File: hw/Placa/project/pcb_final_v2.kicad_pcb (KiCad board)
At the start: 2 copper layers, 22 parts, among them J1 pin_socket-bluepill, J10 tcrt5000_conector_2, J11 tcrt5000_conector_3, J12 tcrt5000_conector_1, J2 pin_socket-bluepill, J9 tof-connector_3, SW2 key, U2 Receptor IR, U4 AMS1117-3.3

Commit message: atualização pcb
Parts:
- removed power_drive1: KRE borne, TerminalBlock_Phoenix:TerminalBlock_Phoenix_MKDS-1,5-2-5.08_1x02_P5.08mm_Horizontal
- moved C2 22.2 mm to (128.0, 68.5), turned to -90 degrees
- moved U4 20.9 mm to (118.0, 72.3)
- moved C_polarized1 17.7 mm to (132.5, 69.5), turned to 90 degrees
- moved D1 14.3 mm to (128.9, 64.0), turned to 90 degrees
- moved L1 9.82 mm to (139.5, 69.5)
- moved D3 9.49 mm to (143.4, 69.5)
- moved C3 9.39 mm to (126.5, 78.5)
- moved SW2 7.29 mm to (134.5, 64.0), turned to 90 degrees
- moved J2 6.86 mm to (147.3, 79.9)
- moved OUT_buck-6V1 2.61 mm to (159.5, 58.5)
- moved IN_buck-7.4V1 2.25 mm to (147.0, 58.5)
- moved J9 1.52 mm to (161.5, 75.8)
- moved tof-connector_2 1.52 mm to (161.5, 95.2)
- moved signal_motors1 1.36 mm to (127.0, 126.5)
- moved J1 1.32 mm to (132.1, 79.9)
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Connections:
- OUT_buck-6V1 pad 1: GNDPWR -> GNDS
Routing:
- net (no net): track 0.00 -> 197.9 mm
- net GNDPWR: track 112.0 -> 38.6 mm
- net I2C1_SCL: track 69.4 -> 0.00 mm, vias 4 -> 0
- net I2C1_SDA: track 68.5 -> 0.00 mm, vias 5 -> 0
- net GNDS: track 138.8 -> 92.3 mm, vias 3 -> 0
- net +3V3: track 142.7 -> 97.2 mm, vias 11 -> 1
- net XSHUT1: track 31.6 -> 0.00 mm
- net XSHUT3: track 27.2 -> 0.00 mm
- net XSHUT2: track 24.8 -> 0.00 mm
- net D4: track 24.6 -> 0.00 mm
- net MB-: track 22.7 -> 0.00 mm
- net IN-BUCK: track 28.4 -> 8.30 mm
- net MB+: track 19.1 -> 0.00 mm
- net D1: track 17.2 -> 0.00 mm
- net D3: track 16.4 -> 0.00 mm
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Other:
- board outline added: 50.7 x 80 mm

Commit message: Atualiza o layout da PCB apos autoroteamento
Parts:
- moved J9 1.52 mm to (160.0, 75.5)
- moved tof-connector_1 1.52 mm to (160.0, 114.5)
- moved tof-connector_2 1.52 mm to (160.0, 95.0)
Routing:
- net (no net): track 197.9 -> 0.00 mm
- net I2C1_SCL: track 0.00 -> 82.4 mm, vias 0 -> 2
- net +3V3: track 97.2 -> 164.7 mm, vias 1 -> 4
- net I2C1_SDA: track 0.00 -> 63.8 mm, vias 0 -> 3
- net XSHUT1: track 0.00 -> 27.0 mm
- net XSHUT3: track 0.00 -> 17.7 mm
- net XSHUT2: track 0.00 -> 14.7 mm
- net +7.4V: track 8.71 -> 22.2 mm, vias 0 -> 1
- net MA+: track 0.00 -> 5.43 mm
- net D2: track 0.00 -> 0.72 mm

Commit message: pcb finalizada
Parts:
- added C1: 4,7uF, Capacitor_SMD:C_0805_2012Metric_Pad1.18x1.45mm_HandSolder, B.Cu at (123.4, 112.8)
- added C4: 100nF, Capacitor_SMD:C_0805_2012Metric_Pad1.18x1.45mm_HandSolder, B.Cu at (123.4, 110.8)
- added R1: 100, Resistor_SMD:R_0805_2012Metric, B.Cu at (114.6, 114.3)
- C2, C3: footprint Capacitor_SMD:C_0805_2012Metric -> Capacitor_SMD:C_0805_2012Metric_Pad1.18x1.45mm_HandSolder
- SW2: footprint Button_Switch_THT:SW_DIP_SPSTx01_Slide_6.7x4.1mm_W7.62mm_P2.54mm_LowProfile -> Button_Switch_THT:SW_CK_JS202011CQN_DPDT_Straight
- moved SW2 2.68 mm to (133.3, 61.6)
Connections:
- 7.4V1 pad 1: +7.4V -> Net-(7.4V1-Pin_1)
- C2 pad 1: GNDPWR -> +5V
- C2 pad 2: +5V -> GNDPWR
- D1 pad 2: +7.4V -> Net-(7.4V1-Pin_1)
- IN_buck-7.4V1 pad 2: IN-BUCK -> +7.4V
- SW2 pad 2: IN-BUCK -> +7.4V
- U4 pad 1: +7.4V -> (no net)
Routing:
- net GNDS: track 92.7 -> 46.0 mm
- net D4: track 0.00 -> 25.1 mm
- net MB-: track 0.00 -> 21.4 mm
- net MB+: track 0.00 -> 17.8 mm
- net D1: track 0.00 -> 17.7 mm
- net D3: track 0.00 -> 16.3 mm
- net MA-: track 0.00 -> 14.2 mm
- net D2: track 0.72 -> 14.5 mm
- net +7.4V: track 22.2 -> 8.87 mm, vias 1 -> 0
- net MA+: track 5.43 -> 16.1 mm
- net Net-(7.4V1-Pin_1): track 0.00 -> 8.71 mm
- net IN-BUCK: track 8.30 -> 0.00 mm
- net +3V3: track 164.7 -> 167.4 mm
- added copper zone on B.Cu, net GNDS
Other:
- board size 50.7 x 80 mm -> 50 x 78.5 mm

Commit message: receptor IR no 5V
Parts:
- removed C4: 100nF, Capacitor_SMD:C_0805_2012Metric_Pad1.18x1.45mm_HandSolder
- added R2: 10k ohm, Resistor_SMD:R_0805_2012Metric, B.Cu at (123.2, 83.6)
- R1: value 100 -> 330 ohm
- moved R1 42.6 mm to (123.2, 72.6)
- moved U2 40.4 mm to (119.3, 80.2), turned to -90 degrees
- moved C1 30.3 mm to (127.2, 82.8), turned to 0 degrees
- moved J10 8.71 mm to (118.8, 102.2)
- moved J11 8.71 mm to (118.8, 114.2)
- moved J12 8.71 mm to (118.7, 90.2)
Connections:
- C1 pad 1: +3V3 -> +5V
- J10 pad 2: D2 -> D3
- J11 pad 2: D3 -> D4
- J12 pad 2: D1 -> D2
- R1 pad 1: +3V3 -> +5V
- R1 pad 2: +3V3 -> Net-(U2-Vs)
- U2 pad 1: D4 -> +5V
- U2 pad 2: +3V3 -> D1
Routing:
- net GNDS: track 46.0 -> 0.58 mm
- net +5V: track 36.5 -> 55.1 mm, vias 0 -> 2
- net +3V3: track 167.4 -> 158.7 mm
- net D4: track 25.1 -> 20.4 mm
- net MA+: track 16.1 -> 12.6 mm
- net D2: track 14.5 -> 16.1 mm
- net D1: track 17.7 -> 18.9 mm
- net D3: track 16.3 -> 15.5 mm
- added copper zone on B.Cu, net (none)
- removed copper zone on B.Cu, net GNDS
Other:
- board size 50 x 78.5 mm -> 100 x 100 mm

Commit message: arquivo step atualizado
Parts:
- turned C2 to 90 degrees
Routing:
- added copper zone on B.Cu, net GNDS
- removed copper zone on B.Cu, net (none)
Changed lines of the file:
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@@
 	(footprint "Capacitor_SMD:C_0805_2012Metric_Pad1.18x1.45mm_HandSolder"
 		(layer "B.Cu")
-		(at 128 68.5 -90)
+		(at 128 68.5 90)
 		(descr "Capacitor SMD 0805 (2012 Metric), square (rectangular) end terminal, IPC-7351 nominal with elongated pad for handsoldering. (Body size source: IPC-SM-782 page 76, https://www.pcb-3d.com/wordpress/wp-content/uploads/ipc-sm-782a_amendment_1_and_2.pdf, https://docs.google.com/spreadsheets/d/1BsfQQcO9C6DZCsRaXUlFlo91Tg2WpOkGARC1WS5S8t0/edit?usp=sharing)")
 		(tags "capacitor handsolder")
@@
 		(duplicate_pad_numbers_are_jumpers no)
 		(fp_line
-			(start -0.261252 0.735)
-			(end 0.261252 0.735)
+			(start -0.261252 -0.735)
+			(end 0.261252 -0.735)
 			(stroke
 				(width 0.12)
@@
 		)
 		(fp_line
-			(start -0.261252 -0.735)
-			(end 0.261252 -0.735)
+			(start -0.261252 0.735)
+			(end 0.261252 0.735)
 			(stroke
 				(width 0.12)
@@
 		)
 		(pad "1" smd roundrect
-			(at -1.0375 0 270)
+			(at -1.0375 0 90)
 			(size 1.175 1.45)
 			(layers "B.Cu" "B.Mask" "B.Paste")
@@
 		)
 		(pad "2" smd roundrect
-			(at 1.0375 0 270)
+			(at 1.0375 0 90)
 			(size 1.175 1.45)
 			(layers "B.Cu" "B.Mask" "B.Paste")
@@
 	)
 	(segment
+		(start 122 58.3275)
+		(end 124.368 58.3275)
+		(width 1.5)
+		(layer "B.Cu")
+		(net "Net-(7.4V1-Pin_2)")
+	)
+	(segment
+		(start 124.368 58.3275)
+		(end 128.855 53.84)
+		(width 1.5)
+		(layer "B.Cu")
+		(net "Net-(7.4V1-Pin_2)")
+	)
+	(segment
 		(start 129 67.5)
 		(end 128.05 67.5)
@@
 		(net "+7.4V")
 	)
-	(segment
-		(start 122 58.3275)
-		(end 124.368 58.3275)
-		(width 1.5)
-		(layer "B.Cu")
-		(net "Net-(7.4V1-Pin_2)")
-	)
-	(segment
-		(start 124.368 58.3275)
-		(end 128.855 53.84)
-		(width 1.5)
-		(layer "B.Cu")
-		(net "Net-(7.4V1-Pin_2)")
-	)
 	(zone
+		(net "GNDS")
 		(layer "B.Cu")
 		(hatch edge 0.5)

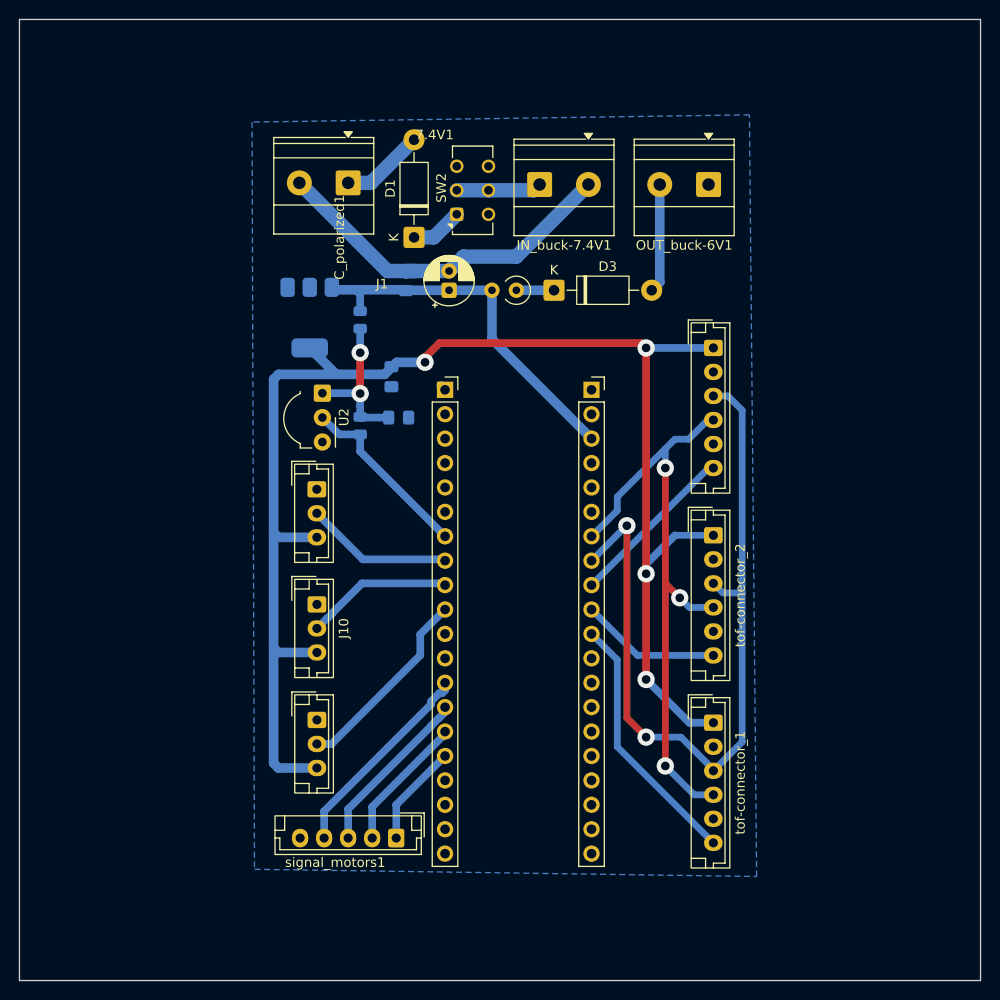
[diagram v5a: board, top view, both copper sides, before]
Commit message: adiçao dos pinos GPIO
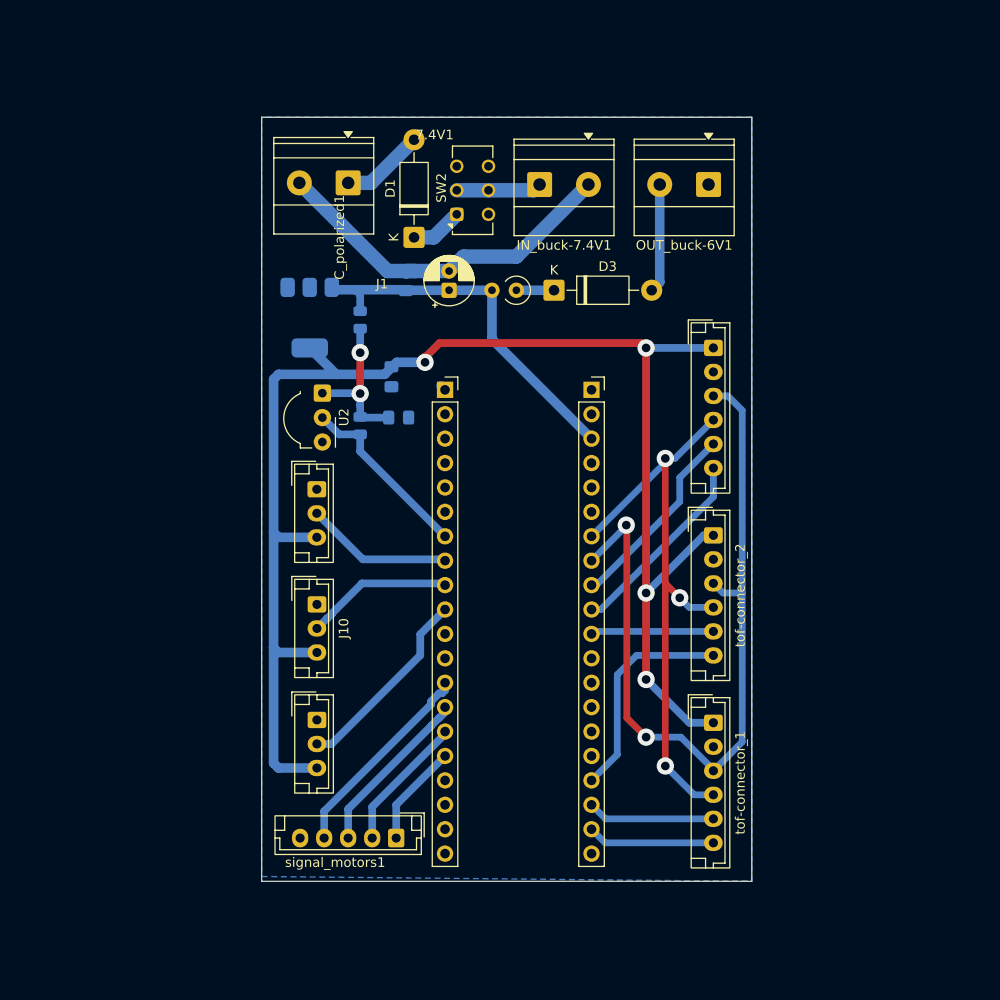
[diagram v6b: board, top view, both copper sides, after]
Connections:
- 7.4V1 pad 1: Net-(7.4V1-Pin_2) -> GNDPWR
- 7.4V1 pad 2: GNDPWR -> Net-(7.4V1-Pin_2)
- C1 pad 1: +5V -> Net-(U2-Vs)
- IN_buck-7.4V1 pad 1: GNDPWR -> +7.4V
- IN_buck-7.4V1 pad 2: +7.4V -> GNDPWR
- J2 pad 10: XSHUT2 -> XSHUT3
- J2 pad 11: XSHUT1 -> GPIO2
- J2 pad 17: unconnected-(J2-Pin_17-Pad17) -> XSHUT2
- J2 pad 18: unconnected-(J2-Pin_18-Pad18) -> GPIO1
- J2 pad 19: unconnected-(J2-Pin_19-Pad19) -> XSHUT1
- J2 pad 9: XSHUT3 -> GPIO3
- J9 pad 5: unconnected-(J9-Pin_5-Pad5) -> GPIO3
- R2 pad 1: +5V -> Net-(U2-Vs)
- U2 pad 1: +5V -> D1
- U2 pad 2: D1 -> Net-(U2-Vs)
- U4 pad 1: (no net) -> GNDPWR
- tof-connector_1 pad 5: unconnected-(tof-connector_1-Pin_5-Pad5) -> GPIO1
- tof-connector_2 pad 5: unconnected-(tof-connector_2-Pin_5-Pad5) -> GPIO2
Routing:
- net GPIO3: track 0.00 -> 20.2 mm
- net XSHUT1: track 27.0 -> 13.3 mm
- net GPIO1: track 0.00 -> 13.3 mm
- net GPIO2: track 0.00 -> 12.8 mm
- net XSHUT2: track 14.7 -> 22.9 mm
- net XSHUT3: track 17.7 -> 21.0 mm
- net I2C1_SDA: track 63.8 -> 62.4 mm
- added copper zone on B.Cu, net (none)
- removed copper zone on B.Cu, net GNDS
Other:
- board size 100 x 100 mm -> 51 x 79.5 mm
